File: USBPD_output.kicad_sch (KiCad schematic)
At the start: 26 parts, among them J2 Bus_RJ45_7499111121A, J3 USB-C_GCT_USB4105-GF-A, U3 INA230AIRGTR, U6 TPS65987DDHRSHR

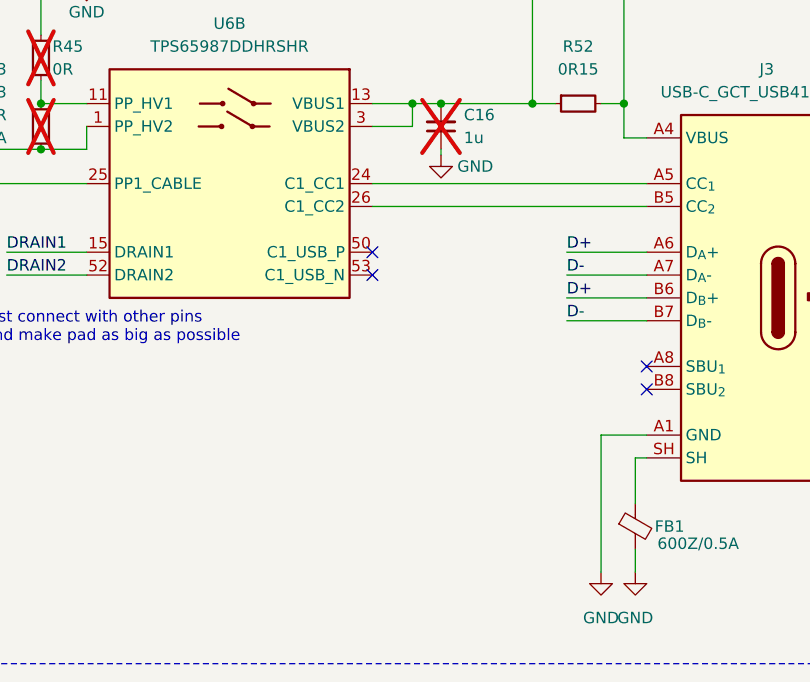
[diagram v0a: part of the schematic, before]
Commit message: [#62835] Add esd protection for usb, add pwr planes, route LS signals
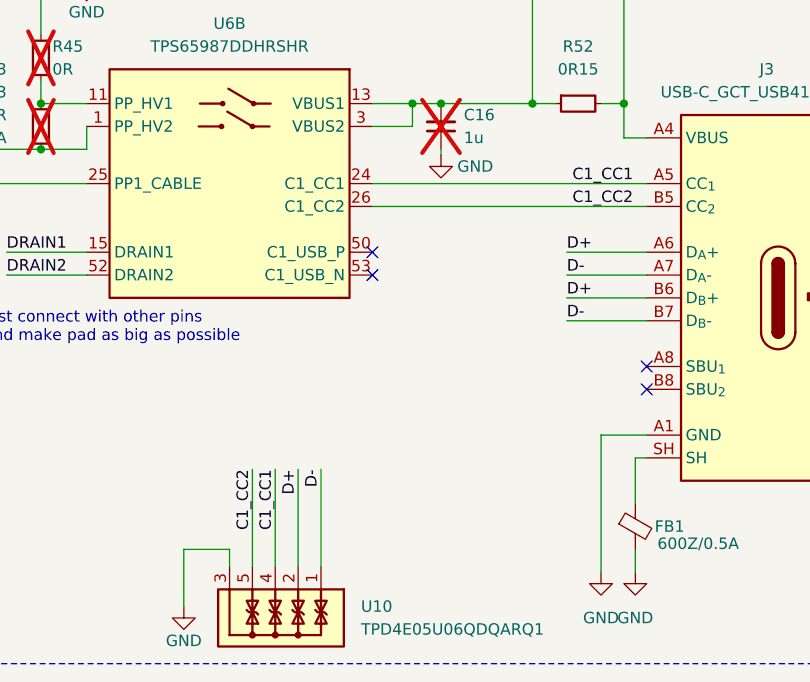
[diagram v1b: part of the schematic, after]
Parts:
- added U10: TPD4E05U06QDQARQ1, antmicro-footprints:USON-10_2.5x1mm_P0.5mm, symbol antmicroTVSDiodes:TPD4E05U06QDQARQ1
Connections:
- net D+: now also U10.2, U10.9
- net D-: now also U10.1, U10.10
- net GND: now also U10.3, U10.8
- net C1_CC1: now reaches J3.A5 (CC_{1}), U6.24 (C1_CC1)
- net C1_CC1: now also U10.4, U10.7
- net C1_CC2: now reaches J3.B5 (CC_{2}), U6.26 (C1_CC2)
- net C1_CC2: now also U10.5, U10.6
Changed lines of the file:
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@@
+    (stroke (width 0) (type default))
+  )
+  (wire (pts (xy 259.715 219.71) (xy 259.715 230.505))
     (stroke (width 0) (type default))
   )
@@
     (stroke (width 0) (type default))
   )
+  (wire (pts (xy 264.795 219.71) (xy 264.795 230.505))
+    (stroke (width 0) (type default))
+  )
   (wire (pts (xy 294.64 200.66) (xy 303.53 200.66))
     (stroke (width 0) (type default))
@@
     (stroke (width 0) (type default))
   )
+  (wire (pts (xy 262.255 219.71) (xy 262.255 230.505))
+    (stroke (width 0) (type default))
+  )
   (wire (pts (xy 241.3 181.61) (xy 241.3 184.15))
     (stroke (width 0) (type default))
@@
     (stroke (width 0) (type default))
   )
+  (wire (pts (xy 257.175 228.6) (xy 252.095 228.6))
+    (stroke (width 0) (type default))
+  )
   (wire (pts (xy 290.83 163.83) (xy 290.83 179.07))
     (stroke (width 0) (type default))
@@
     (stroke (width 0) (type default))
   )
+  (wire (pts (xy 252.095 228.6) (xy 252.095 234.95))
+    (stroke (width 0) (type default))
+  )
   (wire (pts (xy 217.17 196.85) (xy 226.06 196.85))
     (stroke (width 0) (type default))
@@
   )
   (wire (pts (xy 132.08 222.25) (xy 139.7 222.25))
+    (stroke (width 0) (type default))
+  )
+  (wire (pts (xy 267.335 219.71) (xy 267.335 230.505))
+    (stroke (width 0) (type default))
+  )
+  (wire (pts (xy 257.175 230.505) (xy 257.175 228.6))
     (stroke (width 0) (type default))
   )
@@
     (effects (font (size 1.27 1.27)) (justify right bottom))
   )
+  (label "D-" (at 267.335 219.71 270) (fields_autoplaced)
+    (effects (font (size 1.27 1.27)) (justify right bottom))
+  )
   (label "MDI2_P" (at 316.23 66.04 180) (fields_autoplaced)
     (effects (font (size 1.27 1.27)) (justify right bottom))
@@
     (effects (font (size 1.27 1.27)) (justify right bottom))
   )
+  (label "D+" (at 264.795 219.71 270) (fields_autoplaced)
+    (effects (font (size 1.27 1.27)) (justify right bottom))
+  )
   (label "MDI3_P" (at 253.365 96.52 0) (fields_autoplaced)
     (effects (font (size 1.27 1.27)) (justify left bottom))
@@
     (effects (font (size 1.27 1.27)) (justify left bottom))
   )
+  (label "C1_CC1" (at 262.255 219.71 270) (fields_autoplaced)
+    (effects (font (size 1.27 1.27)) (justify right bottom))
+  )
   (label "SDA" (at 189.23 199.39 180) (fields_autoplaced)
     (effects (font (size 1.27 1.27)) (justify right bottom))
@@
     (effects (font (size 1.27 1.27)) (justify left bottom))
   )
+  (label "C1_CC1" (at 295.275 187.96 0) (fields_autoplaced)
+    (effects (font (size 1.27 1.27)) (justify left bottom))
+  )
   (label "SCL" (at 121.92 210.185 270) (fields_autoplaced)
     (effects (font (size 1.27 1.27)) (justify right bottom))
   )
+  (label "C1_CC2" (at 259.715 219.71 270) (fields_autoplaced)
+    (effects (font (size 1.27 1.27)) (justify right bottom))
+  )
   (label "MDI3_N" (at 253.365 99.06 0) (fields_autoplaced)
     (effects (font (size 1.27 1.27)) (justify left bottom))
@@
   )
   (label "MDI2_N" (at 253.365 93.98 0) (fields_autoplaced)
+    (effects (font (size 1.27 1.27)) (justify left bottom))
+  )
+  (label "C1_CC2" (at 295.275 190.5 0) (fields_autoplaced)
     (effects (font (size 1.27 1.27)) (justify left bottom))
   )
@@
     )
   )
+  (symbol (lib_id "antmicropower:GND") (at 252.095 234.95 0) (unit 1)
+    (in_bom yes) (on_board yes) (dnp no)
+    (property "Reference" "#PWR088" (at 260.985 237.49 0)
+      (effects (font (size 1.27 1.27) (thickness 0.15)) (justify left bottom) hide)
+    )
+    (property "Value" "GND" (at 252.095 238.76 0)
+      (effects (font (size 1.27 1.27) (thickness 0.15)))
+    )
+    (property "Footprint" "" (at 260.985 242.57 0)
+      (effects (font (size 1.27 1.27) (thickness 0.15)) (justify left bottom) hide)
+    )
+    (property "Datasheet" "" (at 260.985 247.65 0)
+      (effects (font (size 1.27 1.27) (thickness 0.15)) (justify left bottom) hide)
+    )
+    (property "Author" "Antmicro" (at 260.985 242.57 0)
+      (effects (font (size 1.27 1.27) (thickness 0.15)) (justify left bottom) hide)
+    )
+    (property "License" "Apache-2.0" (at 260.985 245.11 0)
+      (effects (font (size 1.27 1.27) (thickness 0.15)) (justify left bottom) hide)
+    )
+    (pin "1")
+    (instances
+      (project "antmicro-poe-to-usbc-pd-adapter"
+        (path "/cf0d4429-3f03-449f-96a7-26d69371a46d/71fd6a9f-e91f-4e27-909c-676c68ed5a18"
+          (reference "#PWR088") (unit 1)
+        )
+      )
+    )
+  )
   (symbol (lib_id "antmicropower:+3V3") (at 114.3 210.185 0) (unit 1)
     (in_bom yes) (on_board yes) (dnp no)
@@
         )
       )
+    )
+  )
+  (symbol (lib_id "antmicroTVSDiodes:TPD4E05U06QDQARQ1") (at 267.335 230.505 270) (unit 1)
+    (in_bom yes) (on_board yes) (dnp no) (fields_autoplaced)
+    (property "Reference" "U10" (at 271.78 234.95 90)
+      (effects (font (size 1.27 1.27) (thickness 0.15)) (justify left))
+    )
+    (property "Value" "TPD4E05U06QDQARQ1" (at 257.175 254.635 0)
+      (effects (font (size 1.27 1.27) (thickness 0.15)) (justify left bottom) hide)
+    )
+    (property "Footprint" "antmicro-footprints:USON-10_2.5x1mm_P0.5mm" (at 262.255 254.635 0)
+      (effects (font (size 1.27 1.27) (thickness 0.15)) (justify left bottom) hide)
+    )
+    (property "Datasheet" "https://www.ti.com/lit/ds/symlink/tpd4e05u06-q1.pdf?HQS=dis-mous-null-mousermode-dsf-pf-null-wwe&ts=1663591265741&ref_url=https%253A%252F%252Fwww.mouser.com%252F" (at 259.715 254.635 0)
+      (effects (font (size 1.27 1.27) (thickness 0.15)) (justify left bottom) hide)
+    )
+    (property "MPN" "TPD4E05U06QDQARQ1" (at 271.78 237.49 90)
+      (effects (font (size 1.27 1.27) (thickness 0.15)) (justify left))
+    )
+    (property "Manufacturer" "Texas Instruments" (at 254.635 254.635 0)
+      (effects (font (size 1.27 1.27) (thickness 0.15)) (justify left bottom) hide)
+    )
+    (property "Author" "Antmicro" (at 252.095 254.635 0)
+      (effects (font (size 1.27 1.27) (thickness 0.15)) (justify left bottom) hide)
+    )
+    (property "License" "Apache-2.0" (at 249.555 254.635 0)
+      (effects (font (size 1.27 1.27) (thickness 0.15)) (justify left bottom) hide)
+    )
+    (pin "6")
+    (pin "5")
+    (pin "4")
+    (pin "2")
+    (pin "10")
+    (pin "1")
+    (pin "3")
+    (pin "7")
+    (pin "8")
+    (pin "9")
+    (instances
+      (project "antmicro-poe-to-usbc-pd-adapter"
+        (path "/cf0d4429-3f03-449f-96a7-26d69371a46d/71fd6a9f-e91f-4e27-909c-676c68ed5a18"
+          (reference "U10") (unit 1)
+        )
+      )

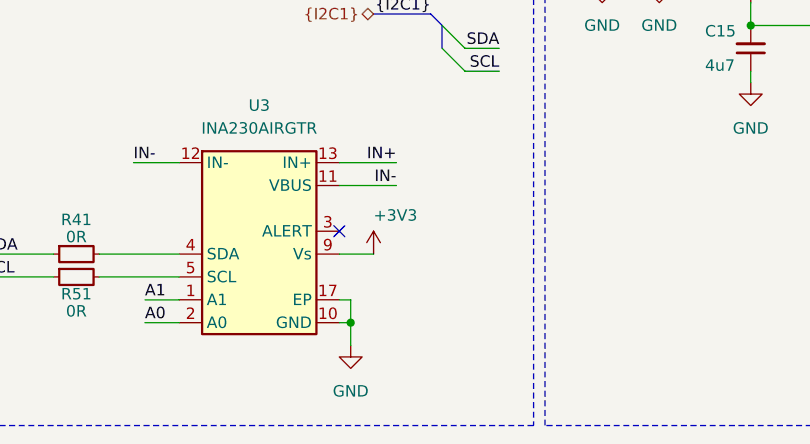
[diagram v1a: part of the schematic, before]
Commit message: [#62835] Tackle DRC problems, change vias size
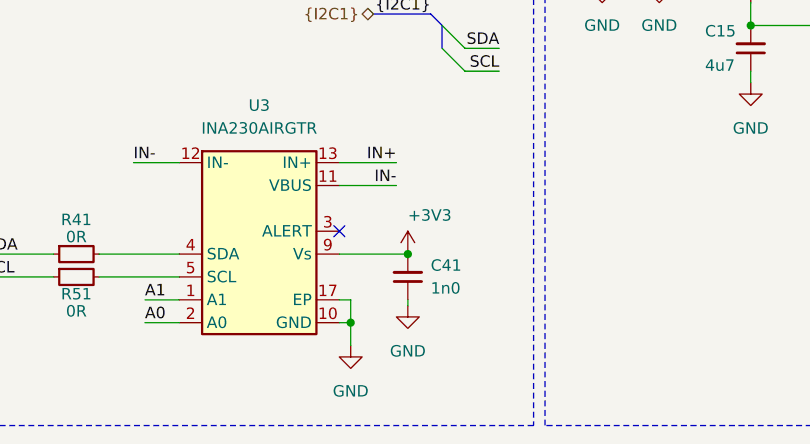
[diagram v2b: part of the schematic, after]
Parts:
- added C41: C_1n0_0402, antmicro-footprints:C_0402_1005Metric, symbol antmicroCapacitors0402:C_1n0_0402
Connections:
- net +3V3: now also C41.2
- net GND: now also C41.1
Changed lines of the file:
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@@
   (junction (at 300.99 179.07) (diameter 0) (color 0 0 0 0)
+  )
+  (junction (at 179.07 222.25) (diameter 0) (color 0 0 0 0)
   )
   (junction (at 101.6 225.425) (diameter 0) (color 0 0 0 0)
@@
     (stroke (width 0) (type default))
   )
+  (wire (pts (xy 179.07 227.33) (xy 179.07 227.965))
+    (stroke (width 0) (type default))
+  )
   (wire (pts (xy 302.26 218.44) (xy 302.26 223.52))
     (stroke (width 0) (type default))
@@
     (stroke (width 0) (type default))
   )
-  (wire (pts (xy 171.45 222.25) (xy 175.26 222.25))
+  (wire (pts (xy 171.45 222.25) (xy 179.07 222.25))
     (stroke (width 0) (type default))
   )
@@
     )
   )
-  (symbol (lib_id "antmicropower:+3V3") (at 175.26 222.25 0) (unit 1)
+  (symbol (lib_id "antmicropower:+3V3") (at 179.07 222.25 0) (unit 1)
     (in_bom yes) (on_board yes) (dnp no) (fields_autoplaced)
-    (property "Reference" "#PWR066" (at 175.26 226.06 0)
-      (effects (font (size 1.27 1.27)) (justify left bottom) hide)
-    )
-    (property "Value" "+3V3" (at 175.26 218.694 0)
+    (property "Reference" "#PWR066" (at 179.07 226.06 0)
+      (effects (font (size 1.27 1.27)) (justify left bottom) hide)
+    )
+    (property "Value" "+3V3" (at 179.07 218.694 0)
       (effects (font (size 1.27 1.27)) (justify left bottom))
     )
-    (property "Footprint" "" (at 175.26 222.25 0)
-      (effects (font (size 1.27 1.27)) (justify left bottom) hide)
-    )
-    (property "Datasheet" "" (at 175.26 222.25 0)
+    (property "Footprint" "" (at 179.07 222.25 0)
+      (effects (font (size 1.27 1.27)) (justify left bottom) hide)
+    )
+    (property "Datasheet" "" (at 179.07 222.25 0)
       (effects (font (size 1.27 1.27)) (justify left bottom) hide)
     )
@@
     )
   )
+  (symbol (lib_id "antmicroCapacitors0402:C_1n0_0402") (at 179.07 227.33 90) (unit 1)
+    (in_bom yes) (on_board yes) (dnp no) (fields_autoplaced)
+    (property "Reference" "C41" (at 181.61 223.5136 90)
+      (effects (font (size 1.27 1.27) (thickness 0.15)) (justify right))
+    )
+    (property "Value" "C_1n0_0402" (at 189.23 207.01 0)
+      (effects (font (size 1.27 1.27) (thickness 0.15)) (justify left bottom) hide)
+    )
+    (property "Footprint" "antmicro-footprints:C_0402_1005Metric" (at 191.77 207.01 0)
+      (effects (font (size 1.27 1.27) (thickness 0.15)) (justify left bottom) hide)
+    )
+    (property "Datasheet" "https://www.we-online.com/components/products/datasheet/885012005018.pdf" (at 194.31 207.01 0)
+      (effects (font (size 1.27 1.27) (thickness 0.15)) (justify left bottom) hide)
+    )
+    (property "MPN" "885012005018" (at 196.85 207.01 0)
+      (effects (font (size 1.27 1.27) (thickness 0.15)) (justify left bottom) hide)
+    )
+    (property "Manufacturer" "Würth Elektronik" (at 199.39 207.01 0)
+      (effects (font (size 1.27 1.27) (thickness 0.15)) (justify left bottom) hide)
+    )
+    (property "License" "Apache-2.0" (at 201.93 207.01 0)
+      (effects (font (size 1.27 1.27) (thickness 0.15)) (justify left bottom) hide)
+    )
+    (property "Author" "Antmicro" (at 204.47 207.01 0)
+      (effects (font (size 1.27 1.27) (thickness 0.15)) (justify left bottom) hide)
+    )
+    (property "Val" "1n0" (at 181.61 226.0536 90)
+      (effects (font (size 1.27 1.27) (thickness 0.15)) (justify right))
+    )
+    (property "Voltage" "" (at 207.01 207.01 0)
+      (effects (font (size 1.27 1.27)) (justify left bottom) hide)
+    )
+    (property "Dielectric" "" (at 209.55 207.01 0)
+      (effects (font (size 1.27 1.27)) (justify left bottom) hide)
+    )
+    (pin "1")
+    (pin "2")
+    (instances
+      (project "antmicro-poe-to-usbc-pd-adapter"
+        (path "/cf0d4429-3f03-449f-96a7-26d69371a46d/71fd6a9f-e91f-4e27-909c-676c68ed5a18"
+          (reference "C41") (unit 1)
+        )
+      )
+    )
+  )
   (symbol (lib_id "antmicropower:GND") (at 248.92 82.55 0) (unit 1)
     (in_bom yes) (on_board yes) (dnp no)
@@
         )
       )
+    )
+  )
+  (symbol (lib_id "antmicropower:GND") (at 179.07 227.965 0) (unit 1)
+    (in_bom yes) (on_board yes) (dnp no) (fields_autoplaced)
+    (property "Reference" "#PWR091" (at 187.96 230.505 0)
+      (effects (font (size 1.27 1.27) (thickness 0.15)) (justify left bottom) hide)
+    )
+    (property "Value" "GND" (at 179.07 233.045 0)
+      (effects (font (size 1.27 1.27) (thickness 0.15)))
+    )
+    (property "Footprint" "" (at 187.96 235.585 0)
+      (effects (font (size 1.27 1.27) (thickness 0.15)) (justify left bottom) hide)
+    )
+    (property "Datasheet" "" (at 187.96 240.665 0)
+      (effects (font (size 1.27 1.27) (thickness 0.15)) (justify left bottom) hide)
+    )
+    (property "Author" "Antmicro" (at 187.96 235.585 0)
+      (effects (font (size 1.27 1.27) (thickness 0.15)) (justify left bottom) hide)
+    )
+    (property "License" "Apache-2.0" (at 187.96 238.125 0)
+      (effects (font (size 1.27 1.27) (thickness 0.15)) (justify left bottom) hide)
+    )
+    (pin "1")
+    (instances
+      (project "antmicro-poe-to-usbc-pd-adapter"
+        (path "/cf0d4429-3f03-449f-96a7-26d69371a46d/71fd6a9f-e91f-4e27-909c-676c68ed5a18"
+          (reference "#PWR091") (unit 1)
+        )
+      )

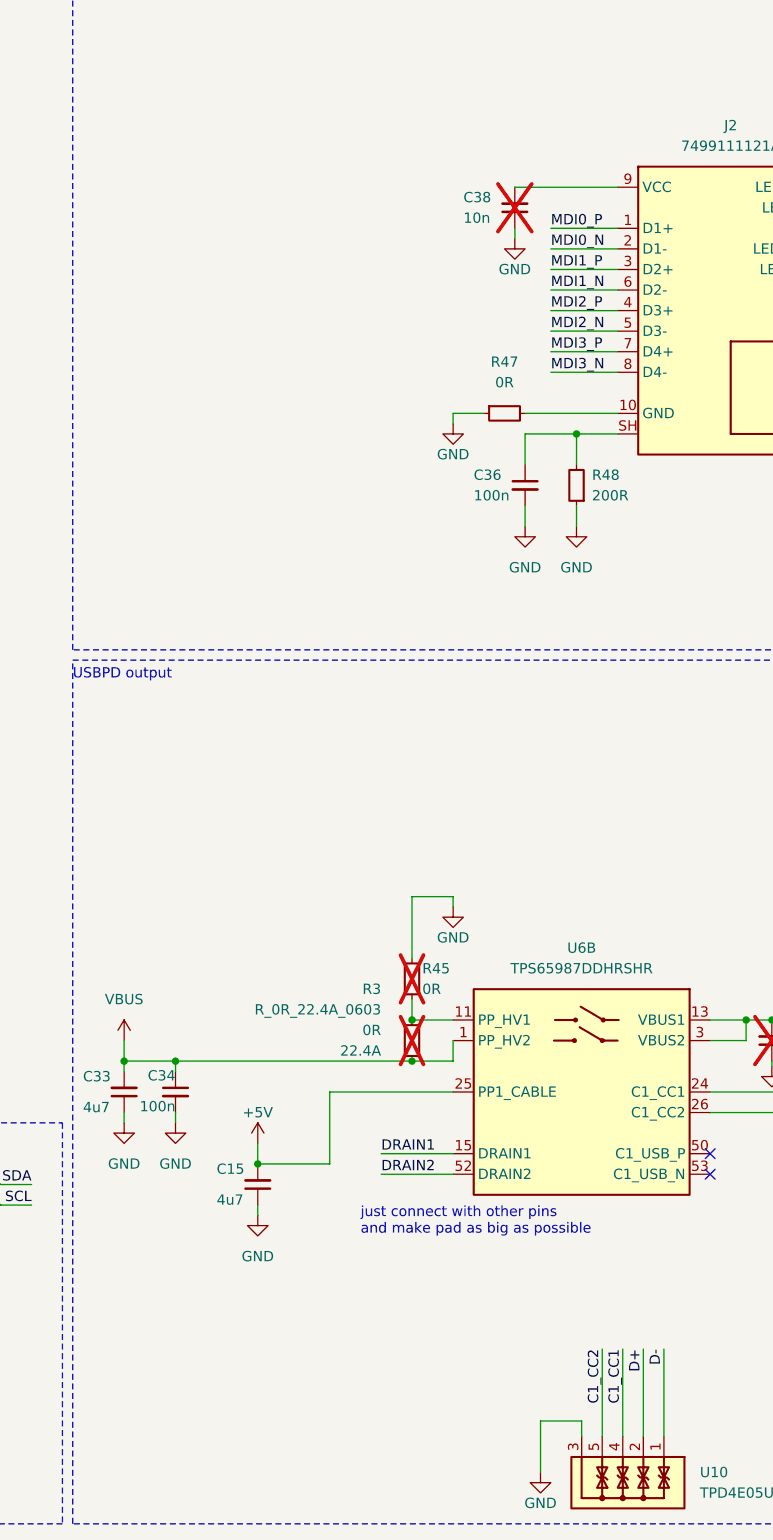
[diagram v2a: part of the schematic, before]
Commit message: [#62835] Tacle ERC problems, add PWR flags
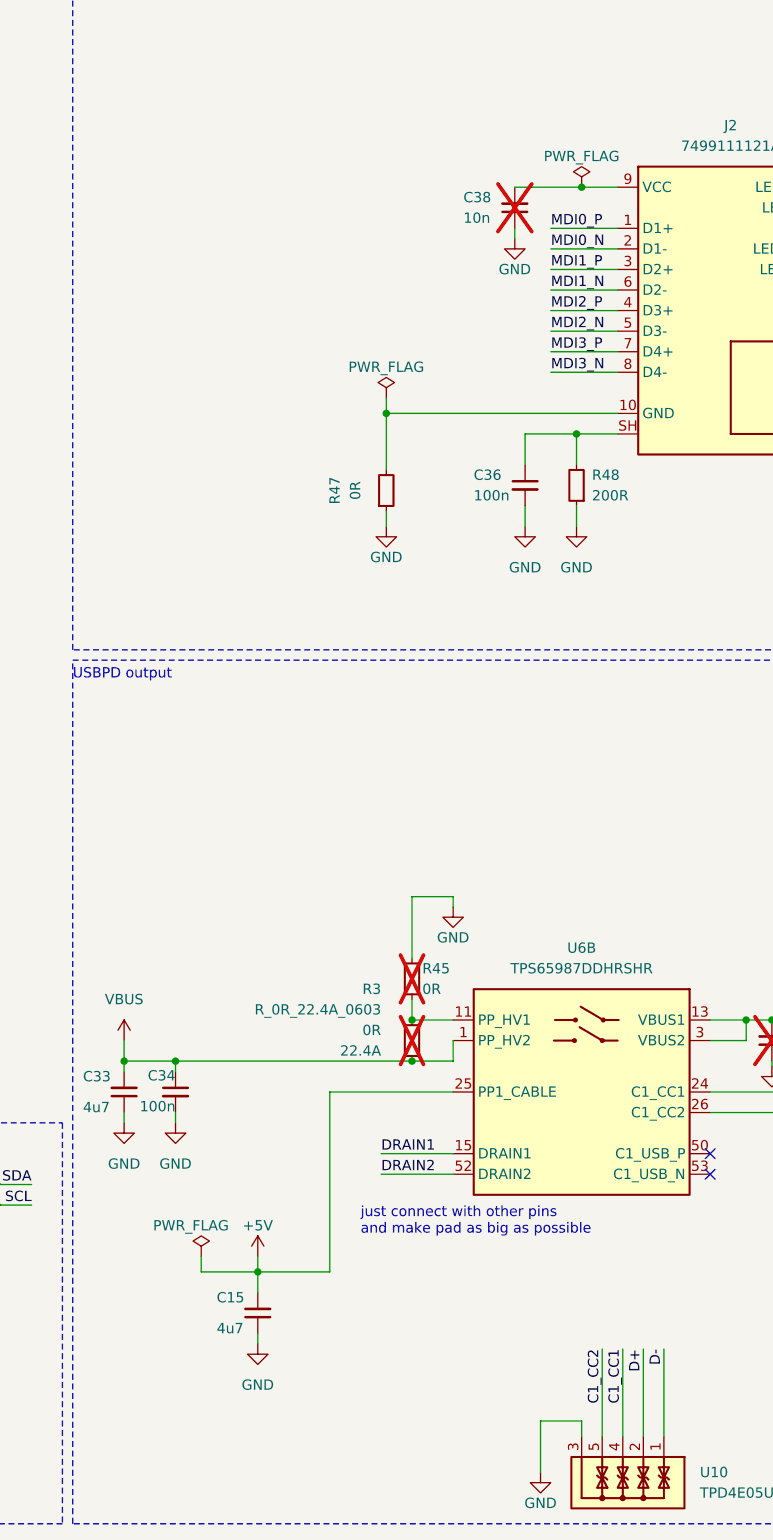
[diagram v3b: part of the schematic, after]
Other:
- moved on the sheet: C15, R47

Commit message: [#62835] PoE to USB-C PD Review Rev.1.0.0 correct points 1,3,4,6,7,11
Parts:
- added C46, C47, C48, C49: C_10n_50V_X7R_0402, antmicro-footprints:C_0402_1005Metric, symbol antmicroCapacitors0402:C_10n_50V_X7R_0402
- added R27: R_270R_0402, antmicro-footprints:R_0402_1005Metric, symbol antmicroResistors0402:R_270R_0402
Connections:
- net +3V3: now also J2.13 (LED2_G+)
- net GND: now also C46.1, C47.1, C48.1, C49.1, R27.1
- net IN+: now also C46.2, C47.2, C48.2, C49.2
- net at J2.14 (LED2_G-): now also R27.2
- no-connect marks 9 -> 7
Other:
- company: (none) -> Antmicro ltd.
- title: (none) -> PoE to USBC PD adapter
- moved on the sheet: C36, C38, FB1, J2, J3, R47, R48, R52

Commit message: [#62835] Add 3V3 LDO to PCB, place CBUS capacitors, change 5V buck layout
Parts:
- removed R27: R_270R_0402, antmicro-footprints:R_0402_1005Metric, symbol antmicroResistors0402:R_270R_0402
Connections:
- net +3V3: no longer J2.13 (LED2_G+)
- net IN+: no longer C46.2, C47.2, C48.2, C49.2
- net IN-: now also C46.2, C47.2, C48.2, C49.2
- no-connect marks 7 -> 9
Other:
- moved on the sheet: C16, C46, C47, C48, C49, FB1, J3, R52

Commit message: [#63274] Change TPS65987 feedback for DCDC gpio pinout
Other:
- moved on the sheet: C15, C16, C33, C34, C46, C47, C48, C49, FB1, J3, R3, R45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
